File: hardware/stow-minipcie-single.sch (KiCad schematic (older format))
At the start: 7 parts

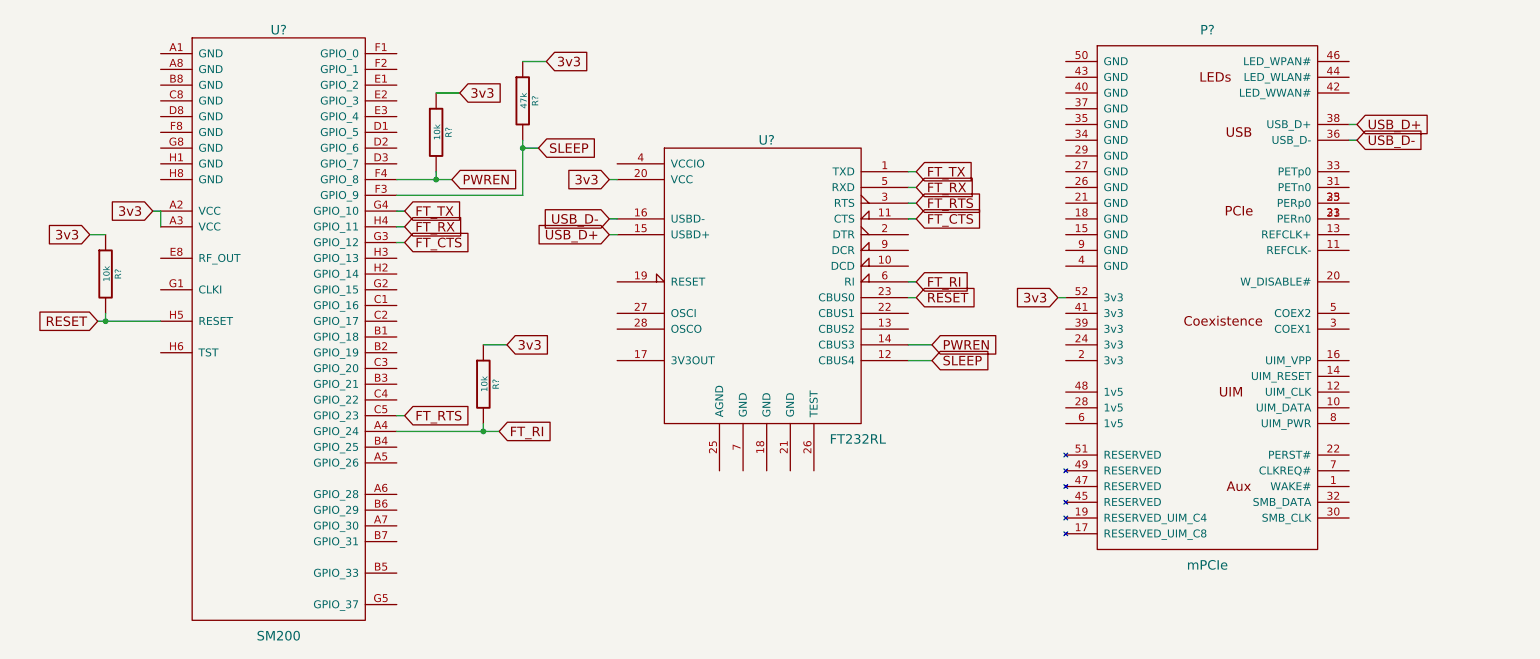
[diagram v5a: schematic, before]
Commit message: Add external xtal for 3v3 operation.
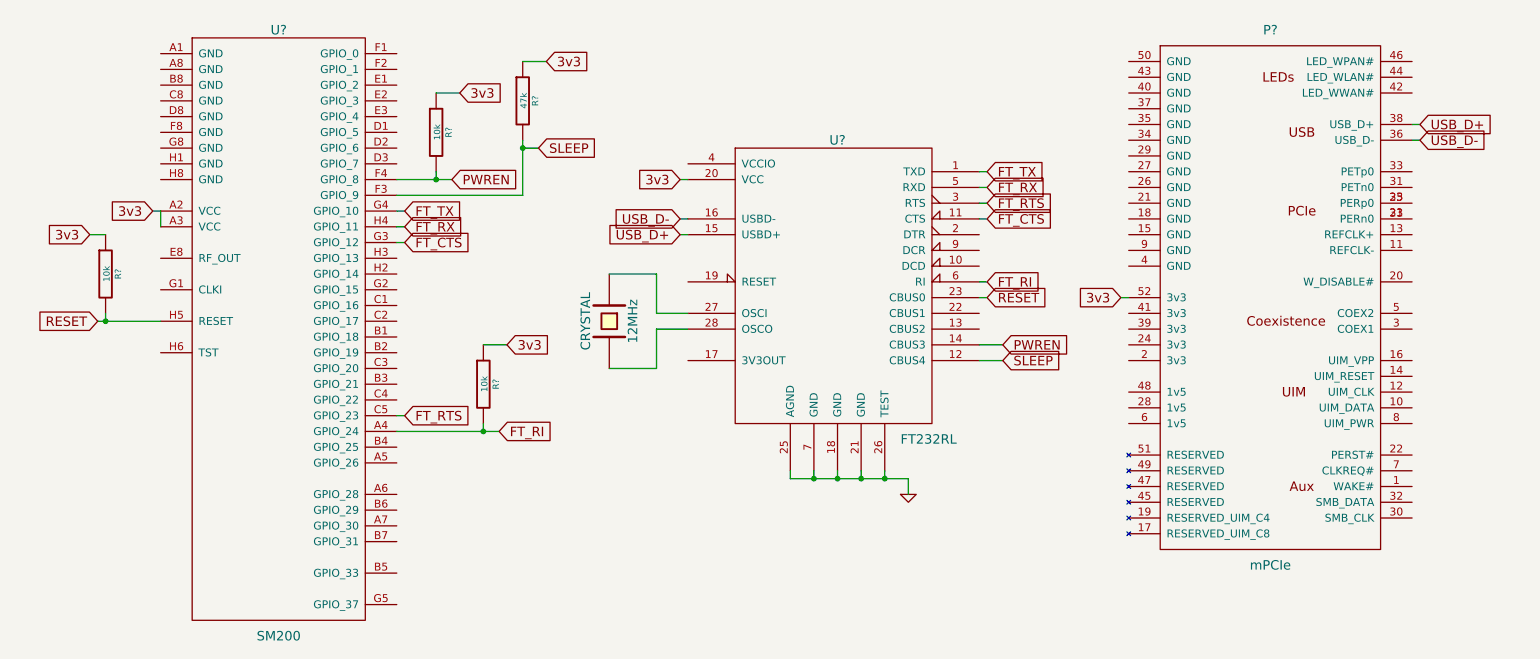
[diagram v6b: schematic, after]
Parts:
- added 12MHz: CRYSTAL, symbol CRYSTAL
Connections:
- net GND: now reaches U?.18 (GND)
- net GND: now also U?.21 (GND), U?.25 (AGND), U?.26 (TEST), U?.7 (GND)
- net at U?.27 (OSCI): now also 12MHz.1
- net at U?.28 (OSCO): now also 12MHz.2
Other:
- moved on the sheet: P?, U?
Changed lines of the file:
@@
 L mPCIe P?
 U 1 1 55C19570
-P 8950 3500
-F 0 "P?" H 8950 4900 60  0000 C CNN
-F 1 "mPCIe" H 8950 1500 60  0000 C CNN
-F 2 "" H 8950 3500 60  0000 C CNN
-F 3 "" H 8950 3500 60  0000 C CNN
-	1    8950 3500
+P 9350 3500
+F 0 "P?" H 9350 4900 60  0000 C CNN
+F 1 "mPCIe" H 9350 1500 60  0000 C CNN
+F 2 "" H 9350 3500 60  0000 C CNN
+F 3 "" H 9350 3500 60  0000 C CNN
+	1    9350 3500
 	1    0    0    -1
 $EndComp
@@
 L FT232RL U?
 U 1 1 55C1978C
-P 6150 3700
-F 0 "U?" H 6150 4600 60  0000 C CNN
-F 1 "FT232RL" H 6550 2700 60  0000 L CNN
-F 2 "" H 6150 3700 60  0000 C CNN
-F 3 "" H 6150 3700 60  0000 C CNN
-	1    6150 3700
-	1    0    0    -1
-$EndComp
-Text GLabel 9900 2700 2    60   Input ~ 0
+P 6600 3700
+F 0 "U?" H 6600 4600 60  0000 C CNN
+F 1 "FT232RL" H 7000 2700 60  0000 L CNN
+F 2 "" H 6600 3700 60  0000 C CNN
+F 3 "" H 6600 3700 60  0000 C CNN
+	1    6600 3700
+	1    0    0    -1
+$EndComp
+Text GLabel 10300 2700 2    60   Input ~ 0
 USB_D+
-Text GLabel 9900 2800 2    60   Input ~ 0
+Text GLabel 10300 2800 2    60   Input ~ 0
 USB_D-
-Text GLabel 5150 3400 0    60   Input ~ 0
+Text GLabel 5600 3400 0    60   Input ~ 0
 USB_D+
-Text GLabel 5150 3300 0    60   Input ~ 0
+Text GLabel 5600 3300 0    60   Input ~ 0
 USB_D-
-Text GLabel 5150 3050 0    60   Input ~ 0
-3v3
-Text GLabel 8000 3800 0    60   Input ~ 0
+Text GLabel 5600 3050 0    60   Input ~ 0
+3v3
+Text GLabel 8400 3800 0    60   Input ~ 0
 3v3
 Text GLabel 2250 3250 0    60   Input ~ 0
 3v3
 Wire Wire Line
-	5150 3300 5200 3300
-Wire Wire Line
-	5150 3400 5200 3400
-Wire Wire Line
-	9850 2700 9900 2700
-Wire Wire Line
-	9850 2800 9900 2800
-Wire Wire Line
-	8000 3800 8050 3800
-Wire Wire Line
-	5150 3050 5200 3050
+	5600 3300 5650 3300
+Wire Wire Line
+	5600 3400 5650 3400
+Wire Wire Line
+	10250 2700 10300 2700
+Wire Wire Line
+	10250 2800 10300 2800
+Wire Wire Line
+	8400 3800 8450 3800
+Wire Wire Line
+	5600 3050 5650 3050
 Wire Wire Line
 	2250 3250 2300 3250
 Wire Wire Line
 	2300 3250 2300 3350
-Text GLabel 7100 3000 2    60   Input ~ 0
+Text GLabel 7550 3000 2    60   Input ~ 0
 FT_TX
-Text GLabel 7100 3100 2    60   Input ~ 0
+Text GLabel 7550 3100 2    60   Input ~ 0
 FT_RX
 Wire Wire Line
-	7050 3000 7100 3000
-Wire Wire Line
-	7100 3100 7050 3100
+	7500 3000 7550 3000
+Wire Wire Line
+	7550 3100 7500 3100
 Text GLabel 3850 3250 2    60   Input ~ 0
 FT_TX
 Text GLabel 3850 3350 2    60   Input ~ 0
 FT_RX
-Text GLabel 7100 3300 2    60   Input ~ 0
+Text GLabel 7550 3300 2    60   Input ~ 0
 FT_CTS
-Text GLabel 7100 3200 2    60   Input ~ 0
+Text GLabel 7550 3200 2    60   Input ~ 0
 FT_RTS
 Wire Wire Line
-	7050 3200 7100 3200
-Wire Wire Line
-	7100 3300 7050 3300
+	7500 3200 7550 3200
+Wire Wire Line
+	7550 3300 7500 3300
 Text GLabel 3850 4550 2    60   Input ~ 0
 FT_RTS
@@
 Wire Wire Line
 	3800 4550 3850 4550
-Text GLabel 7100 3700 2    60   Input ~ 0
+Text GLabel 7550 3700 2    60   Input ~ 0
 FT_RI
 Wire Wire Line
-	7050 3700 7100 3700
+	7500 3700 7550 3700
 Text GLabel 4450 4650 2    60   Input ~ 0
 FT_RI
@@
 Wire Wire Line
 	4350 4100 4500 4100
-Text GLabel 7100 3800 2    60   Input ~ 0
+Text GLabel 7550 3800 2    60   Input ~ 0
 RESET
 Wire Wire Line
-	7050 3800 7100 3800
+	7500 3800 7550 3800
 Text GLabel 1900 3950 0    60   Input ~ 0
 RESET
@@
 Wire Wire Line
 	1850 3400 1950 3400
-Text GLabel 7200 4100 2    60   Input ~ 0
+Text GLabel 7650 4100 2    60   Input ~ 0
 PWREN
-Text GLabel 7200 4200 2    60   Input ~ 0
+Text GLabel 7650 4200 2    60   Input ~ 0
 SLEEP
 Text GLabel 4150 3050 2    60   Input ~ 0
@@
 	3800 3050 4150 3050
 Wire Wire Line
-	7050 4100 7200 4100
-Wire Wire Line
-	7050 4200 7200 4200
+	7500 4100 7650 4100
+Wire Wire Line
+	7500 4200 7650 4200
 Text GLabel 4700 2850 2    60   Input ~ 0
 SLEEP
@@
 Wire Wire Line
 	4600 3150 3800 3150
+Wire Wire Line
+	6450 4900 6450 4950
+Wire Wire Line
+	6300 4950 7050 4950
+Wire Wire Line
+	6600 4950 6600 4900
+Wire Wire Line
+	6750 4950 6750 4900
+Connection ~ 6600 4950
+Wire Wire Line
+	6900 4950 6900 4900
+Connection ~ 6750 4950
+Wire Wire Line
+	6300 4950 6300 4900
+Connection ~ 6450 4950
+$Comp
+L GND #PWR?
+U 1 1 55FA69F7
+P 7050 5050
+F 0 "#PWR?" H 7050 5050 30  0001 C CNN
+F 1 "GND" H 7050 4980 30  0001 C CNN
+F 2 "" H 7050 5050 60  0000 C CNN
+F 3 "" H 7050 5050 60  0000 C CNN
+	1    7050 5050
+	1    0    0    -1
+$EndComp
+Wire Wire Line
+	7050 4950 7050 5050
+Connection ~ 6900 4950
+$Comp
+L CRYSTAL 12MHz
+U 1 1 55FA6B1E
+P 5150 3950
+F 0 "12MHz" H 5150 4100 60  0000 C CNN
+F 1 "CRYSTAL" H 5150 3800 60  0000 C CNN
+F 2 "" H 5150 3950 60  0000 C CNN
+F 3 "" H 5150 3950 60  0000 C CNN
+	1    5150 3950
+	0    1    1    0
+$EndComp
+Wire Wire Line
+	5150 3650 5450 3650
+Wire Wire Line
+	5450 3650 5450 3900
+Wire Wire Line
+	5450 3900 5650 3900
+Wire Wire Line
+	5150 4250 5450 4250
+Wire Wire Line
+	5450 4250 5450 4000
+Wire Wire Line
+	5450 4000 5650 4000
 $EndSCHEMATC

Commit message: Wire up some power connections.
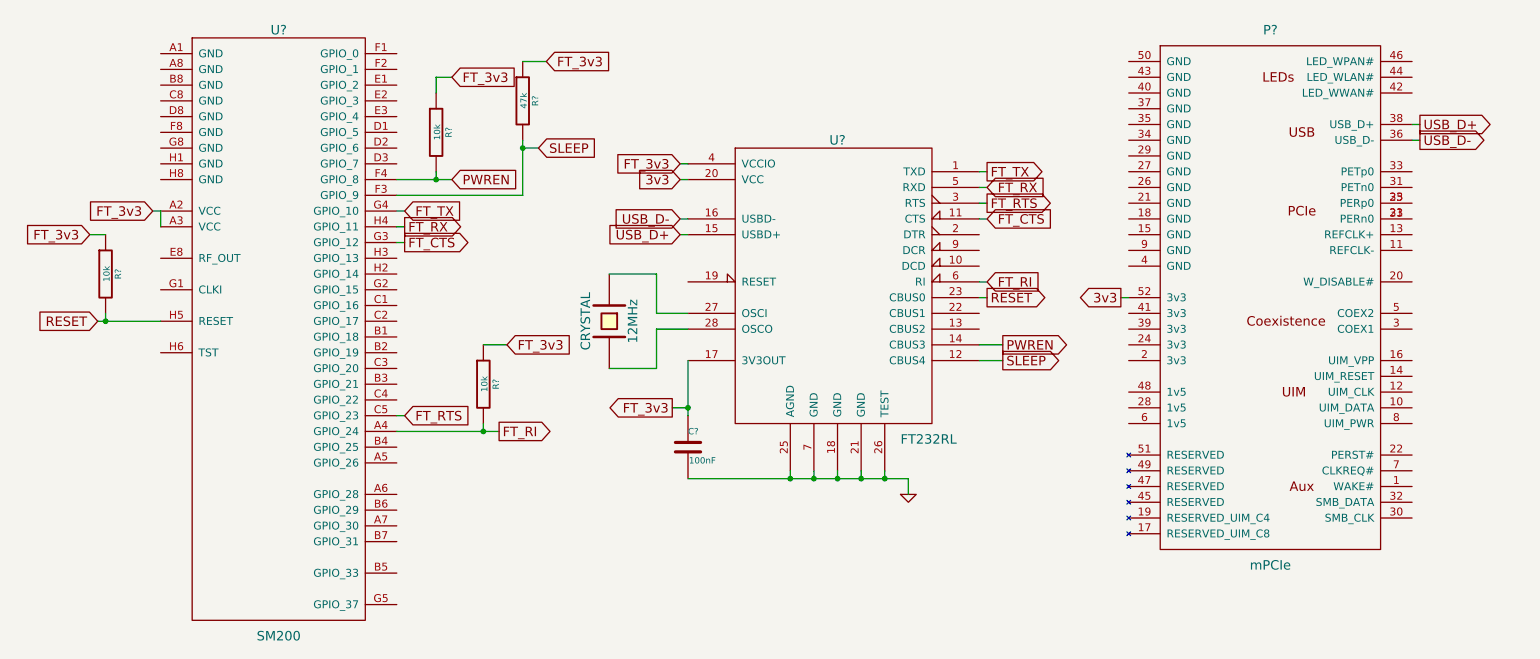
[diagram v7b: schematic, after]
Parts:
- added C?: 100nF, symbol C
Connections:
- net 3v3: no longer R?.1, R?.1, R?.1, R?.1, U?.A2 (VCC), U?.A3 (VCC)
- net GND: now also C?.2
- net FT_3v3: now reaches U?.17 (3V3OUT)
- net FT_3v3: now also R?.1, R?.1, R?.1, R?.1, U?.4 (VCCIO), U?.A2 (VCC), U?.A3 (VCC), C?.1
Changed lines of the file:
@@
 	1    0    0    -1
 $EndComp
-Text GLabel 10300 2700 2    60   Input ~ 0
+Text GLabel 10300 2700 2    60   Output ~ 0
 USB_D+
-Text GLabel 10300 2800 2    60   Input ~ 0
+Text GLabel 10300 2800 2    60   Output ~ 0
 USB_D-
 Text GLabel 5600 3400 0    60   Input ~ 0
@@
 Text GLabel 5600 3050 0    60   Input ~ 0
 3v3
-Text GLabel 8400 3800 0    60   Input ~ 0
+Text GLabel 8400 3800 0    60   Output ~ 0
 3v3
 Text GLabel 2250 3250 0    60   Input ~ 0
-3v3
+FT_3v3
 Wire Wire Line
 	5600 3300 5650 3300
@@
 Wire Wire Line
 	2300 3250 2300 3350
-Text GLabel 7550 3000 2    60   Input ~ 0
+Text GLabel 7550 3000 2    60   Output ~ 0
 FT_TX
 Text GLabel 7550 3100 2    60   Input ~ 0
@@
 Text GLabel 3850 3250 2    60   Input ~ 0
 FT_TX
-Text GLabel 3850 3350 2    60   Input ~ 0
+Text GLabel 3850 3350 2    60   Output ~ 0
 FT_RX
 Text GLabel 7550 3300 2    60   Input ~ 0
 FT_CTS
-Text GLabel 7550 3200 2    60   Input ~ 0
+Text GLabel 7550 3200 2    60   Output ~ 0
 FT_RTS
 Wire Wire Line
@@
 Text GLabel 3850 4550 2    60   Input ~ 0
 FT_RTS
-Text GLabel 3850 3450 2    60   Input ~ 0
+Text GLabel 3850 3450 2    60   Output ~ 0
 FT_CTS
 Wire Wire Line
@@
 Wire Wire Line
 	7500 3700 7550 3700
-Text GLabel 4450 4650 2    60   Input ~ 0
+Text GLabel 4450 4650 2    60   Output ~ 0
 FT_RI
 $Comp
@@
 	4350 4650 4350 4600
 Text GLabel 4500 4100 2    60   Input ~ 0
-3v3
+FT_3v3
 Wire Wire Line
 	4350 4100 4500 4100
-Text GLabel 7550 3800 2    60   Input ~ 0
+Text GLabel 7550 3800 2    60   Output ~ 0
 RESET
 Wire Wire Line
@@
 $EndComp
 Text GLabel 1850 3400 0    60   Input ~ 0
-3v3
+FT_3v3
 Wire Wire Line
 	1900 3950 2300 3950
@@
 Wire Wire Line
 	1850 3400 1950 3400
-Text GLabel 7650 4100 2    60   Input ~ 0
+Text GLabel 7650 4100 2    60   Output ~ 0
 PWREN
-Text GLabel 7650 4200 2    60   Input ~ 0
+Text GLabel 7650 4200 2    60   Output ~ 0
 SLEEP
 Text GLabel 4150 3050 2    60   Input ~ 0
@@
 Wire Wire Line
 	4050 3050 4050 3000
-Text GLabel 4200 2500 2    60   Input ~ 0
-3v3
-Wire Wire Line
-	4050 2500 4200 2500
+Text GLabel 4150 2400 2    60   Input ~ 0
+FT_3v3
 Wire Wire Line
 	3800 3050 4150 3050
@@
 	4600 2800 4600 3150
 Text GLabel 4750 2300 2    60   Input ~ 0
-3v3
+FT_3v3
 Wire Wire Line
 	4600 2300 4750 2300
@@
 	6450 4900 6450 4950
 Wire Wire Line
-	6300 4950 7050 4950
+	5650 4950 7050 4950
 Wire Wire Line
 	6600 4950 6600 4900
@@
 Wire Wire Line
 	5450 4000 5650 4000
+Text GLabel 5550 4500 0    60   Output ~ 0
+FT_3v3
+Wire Wire Line
+	5650 4200 5650 4550
+Wire Wire Line
+	5550 4500 5650 4500
+$Comp
+L C C?
+U 1 1 55FF0BD6
+P 5650 4750
+F 0 "C?" H 5650 4850 40  0000 L CNN
+F 1 "100nF" H 5656 4665 40  0000 L CNN
+F 2 "" H 5688 4600 30  0000 C CNN
+F 3 "" H 5650 4750 60  0000 C CNN
+	1    5650 4750
+	1    0    0    -1
+$EndComp
+Connection ~ 5650 4500
+Connection ~ 6300 4950
+Text GLabel 5600 2950 0    60   Input ~ 0
+FT_3v3
+Wire Wire Line
+	5650 2950 5600 2950
+Wire Wire Line
+	4050 2500 4050 2400
+Wire Wire Line
+	4050 2400 4150 2400
 $EndSCHEMATC

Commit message: Wire up status LED signals.
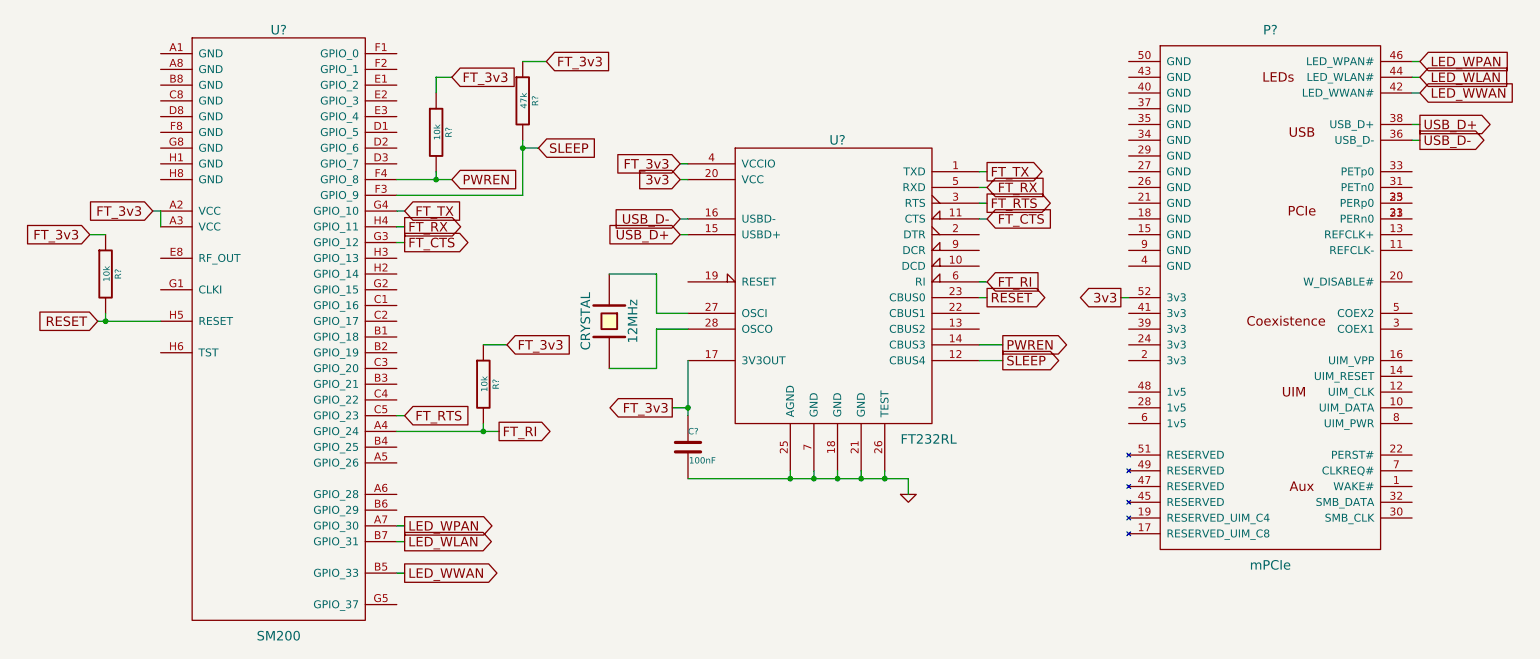
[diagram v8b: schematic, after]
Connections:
- net LED_WPAN: now reaches U?.A7 (GPIO_30)
- net LED_WPAN: now also P?.46 (LED_WPAN#)
- net LED_WWAN: now reaches U?.B5 (GPIO_33)
- net LED_WWAN: now also P?.42 (LED_WWAN#)
- net LED_WLAN: now reaches U?.B7 (GPIO_31)
- net LED_WLAN: now also P?.44 (LED_WLAN#)
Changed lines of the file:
@@
 Wire Wire Line
 	4050 2400 4150 2400
+Text GLabel 10300 2300 2    60   Input ~ 0
+LED_WPAN
+Text GLabel 10300 2400 2    60   Input ~ 0
+LED_WLAN
+Text GLabel 10300 2500 2    60   Input ~ 0
+LED_WWAN
+Wire Wire Line
+	10250 2500 10300 2500
+Wire Wire Line
+	10250 2400 10300 2400
+Wire Wire Line
+	10250 2300 10300 2300
+Text GLabel 3850 5550 2    60   Output ~ 0
+LED_WWAN
+Text GLabel 3850 5350 2    60   Output ~ 0
+LED_WLAN
+Text GLabel 3850 5250 2    60   Output ~ 0
+LED_WPAN
+Wire Wire Line
+	3800 5250 3850 5250
+Wire Wire Line
+	3800 5350 3850 5350
+Wire Wire Line
+	3800 5550 3850 5550
 $EndSCHEMATC
